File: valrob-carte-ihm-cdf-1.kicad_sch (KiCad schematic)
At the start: 42 parts, among them J1 USB_C_Receptacle_USB2.0_14P, J2 Conn_01x02, J3 Conn_01x02, J4 Conn_01x04_Pin, J5 Conn_01x04_Pin, J6 Conn_01x04_Pin, SW1 SW_Push, SW2 SW_Push, SW3 SW_DIP_x04, U1 TLV75733PDBV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

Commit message: pcb: add display buttons routing
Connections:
- net SCL: now also U4.15 (GPIO3/TOUCH3/ADC1_CH2); no longer U4.12 (GPIO8/TOUCH8/ADC1_CH7/SUBSPICS1)

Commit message: pcb: add toggle switch routing
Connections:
- net RGB_LEDS: now also U4.22 (GPIO14/TOUCH14/ADC2_CH3/FSPIWP/FSPIDQS/SUBSPIWP); no longer U4.18 (GPIO10/TOUCH10/ADC1_CH9/FSPICS0/FSPIIO4/SUBSPICS0)
- net Switches/ESW2: now also U4.21 (GPIO13/TOUCH13/ADC2_CH2/FSPIQ/FSPIIO7/SUBSPIQ); no longer U4.20 (GPIO12/TOUCH12/ADC2_CH1/FSPICLK/FSPIIO6/SUBSPICLK)
- net Switches/ESW3: now also U4.20 (GPIO12/TOUCH12/ADC2_CH1/FSPICLK/FSPIIO6/SUBSPICLK); no longer U4.21 (GPIO13/TOUCH13/ADC2_CH2/FSPIQ/FSPIIO7/SUBSPIQ)
- net Switches/ESW4: now also U4.18 (GPIO10/TOUCH10/ADC1_CH9/FSPICS0/FSPIIO4/SUBSPICS0); no longer U4.22 (GPIO14/TOUCH14/ADC2_CH3/FSPIWP/FSPIDQS/SUBSPIWP)

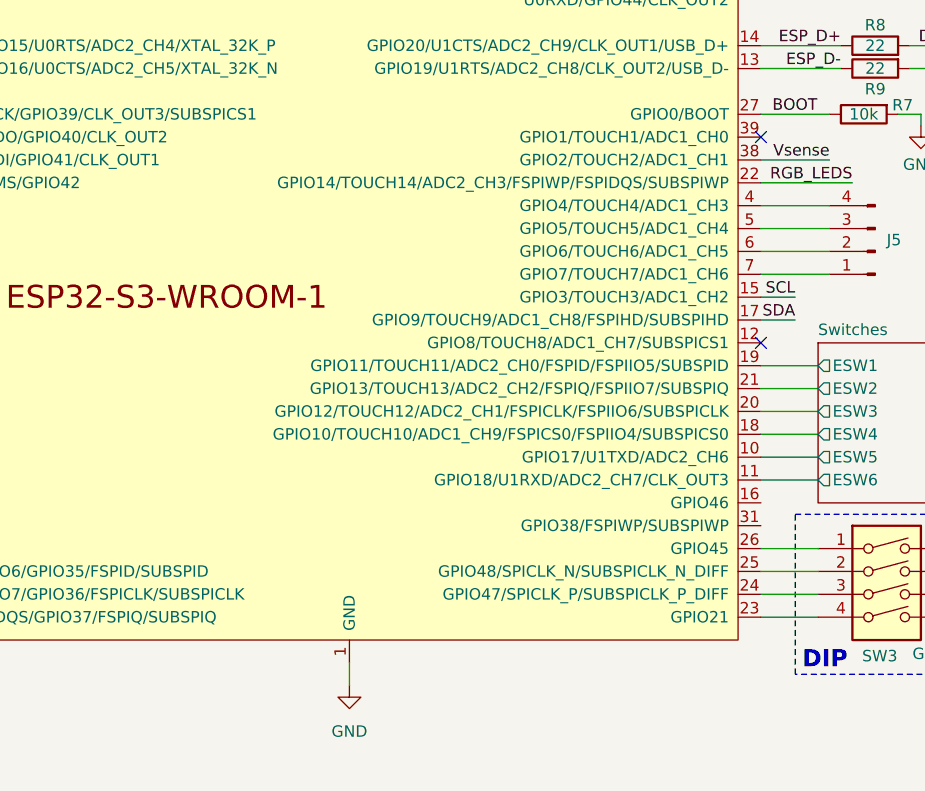
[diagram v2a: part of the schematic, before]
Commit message: pcb: add DIP switches routing
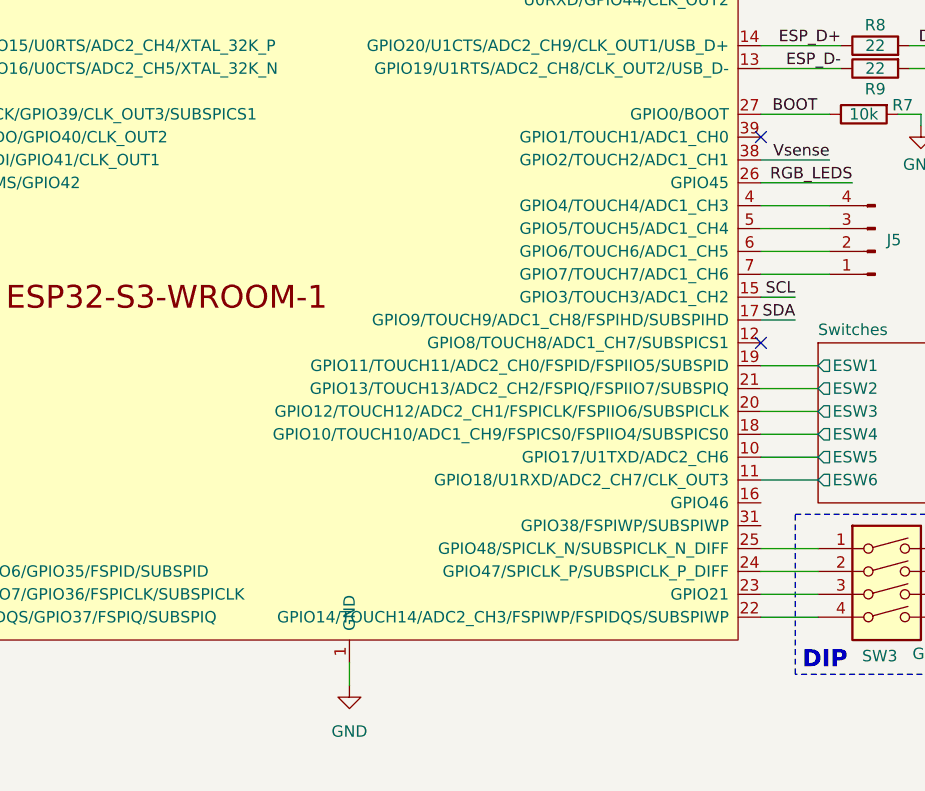
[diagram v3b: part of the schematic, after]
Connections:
- net RGB_LEDS: now also U4.26 (GPIO45); no longer U4.22 (GPIO14/TOUCH14/ADC2_CH3/FSPIWP/FSPIDQS/SUBSPIWP)
- net at SW3.4: now also U4.22 (GPIO14/TOUCH14/ADC2_CH3/FSPIWP/FSPIDQS/SUBSPIWP); no longer U4.23 (GPIO21)
- net at SW3.3: now also U4.23 (GPIO21); no longer U4.24 (GPIO47/SPICLK_P/SUBSPICLK_P_DIFF)
- net at SW3.2: now also U4.24 (GPIO47/SPICLK_P/SUBSPICLK_P_DIFF); no longer U4.25 (GPIO48/SPICLK_N/SUBSPICLK_N_DIFF)
- net at SW3.1: now also U4.25 (GPIO48/SPICLK_N/SUBSPICLK_N_DIFF); no longer U4.26 (GPIO45)

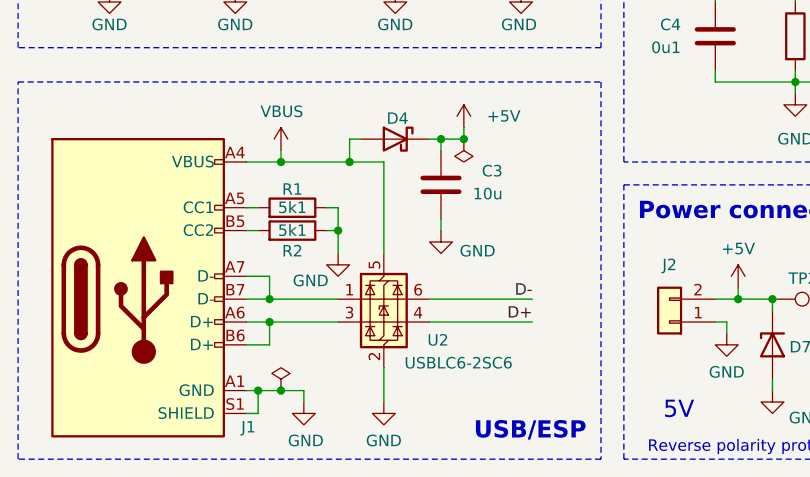
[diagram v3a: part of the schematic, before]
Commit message: switch ST usb ESD to H5VU10U tvs diodes
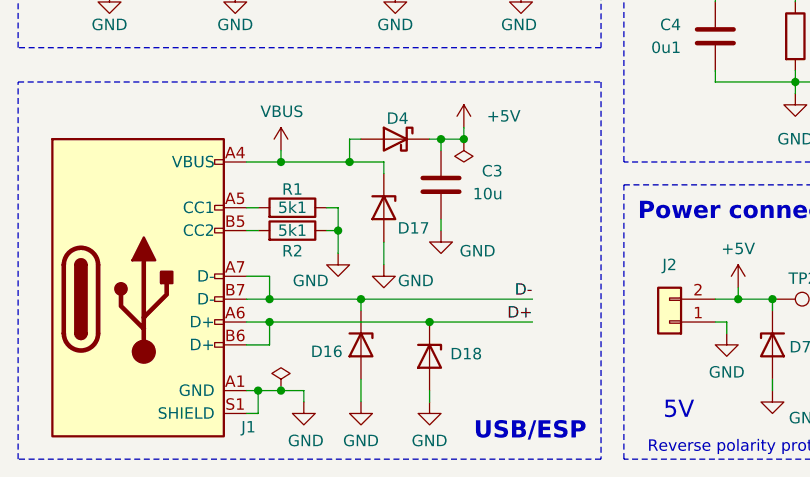
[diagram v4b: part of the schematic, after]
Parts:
- removed U2: USBLC6-2SC6, Package_TO_SOT_SMD:SOT-23-6, symbol Power_Protection:USBLC6-2SC6
- added D16, D17, D18: H5VU10U, Pers:Diode_DFN1006, symbol Pers:H5VU10U
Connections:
- net D+: now also J1.A6 (D+), J1.B6 (D+), D18.1 (K)
- net D-: now also J1.A7 (D-), J1.B7 (D-), D16.1 (K)
- net GND: now also D16.2 (A), D17.2 (A), D18.2 (A)
- net VBUS: now also D17.1 (K)

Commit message: add production files
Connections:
- no-connect marks 8 -> 10
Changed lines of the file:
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@@
+	)
+	(no_connect
+		(at 246.38 115.57)
 	)
 	(no_connect
@@
 	)
 	(no_connect
+		(at 246.38 118.11)
+	)
+	(no_connect

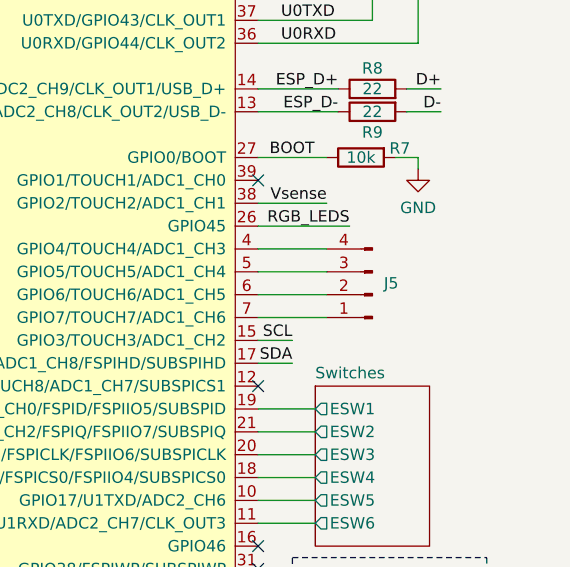
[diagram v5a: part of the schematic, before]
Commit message: pcb/schem: add missing i2c external pullups
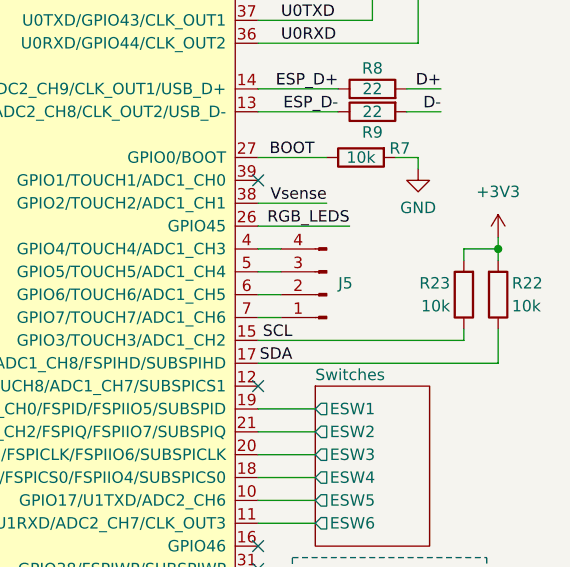
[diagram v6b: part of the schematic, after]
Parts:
- added R22, R23: 10k, Resistor_SMD:R_0402_1005Metric, symbol Device:R
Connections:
- net +3V3: now also R22.2, R23.2
- net SCL: now also R23.1
- net SDA: now also R22.1
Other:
- moved on the sheet: J5

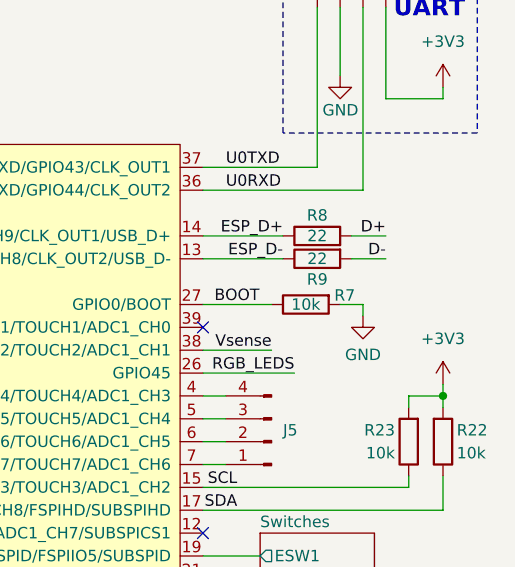
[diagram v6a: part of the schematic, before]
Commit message: pcb/schem: fix BOOT pullup
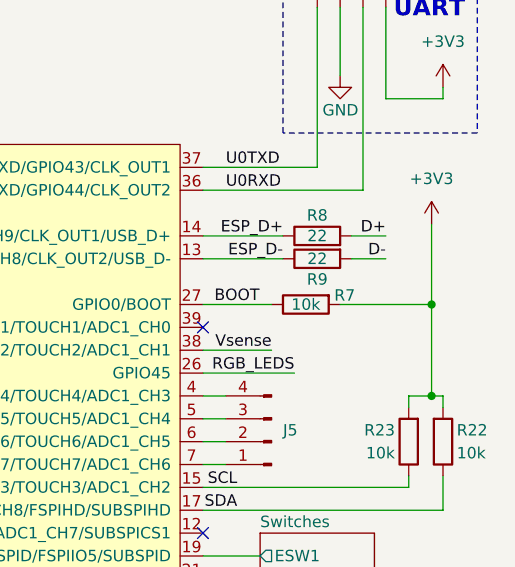
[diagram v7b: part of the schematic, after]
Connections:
- net +3V3: now also R7.2
- net GND: no longer R7.2
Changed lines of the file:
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@@
 	)
 	(junction
-		(at 273.05 82.55)
+		(at 271.78 82.55)
 		(diameter 0)
 		(color 0 0 0 0)
@@
 	)
 	(junction
+		(at 271.78 72.39)
+		(diameter 0)
+		(color 0 0 0 0)
+	)
+	(junction
 		(at 50.8 168.91)
 		(diameter 0)
@@
 	(wire
 		(pts
+			(xy 261.62 72.39) (xy 271.78 72.39)
+		)
+		(stroke
+			(width 0)
+			(type default)
+		)
+	)
+	(wire
+		(pts
 			(xy 246.38 125.73) (xy 252.73 125.73)
 		)
@@
 	(wire
 		(pts
+			(xy 271.78 72.39) (xy 271.78 82.55)
+		)
+		(stroke
+			(width 0)
+			(type default)
+		)
+	)
+	(wire
+		(pts
 			(xy 50.8 125.73) (xy 50.8 130.81)
 		)
@@
 	(wire
 		(pts
-			(xy 273.05 81.28) (xy 273.05 82.55)
+			(xy 271.78 63.5) (xy 271.78 72.39)
 		)
 		(stroke
@@
 	(wire
 		(pts
-			(xy 264.16 73.66) (xy 264.16 72.39)
-		)
-		(stroke
-			(width 0)
-			(type default)
-		)
-	)
-	(wire
-		(pts
 			(xy 64.77 158.75) (xy 64.77 157.48)
 		)
@@
 	(wire
 		(pts
-			(xy 264.16 72.39) (xy 261.62 72.39)
-		)
-		(stroke
-			(width 0)
-			(type default)
-		)
-	)
-	(wire
-		(pts
 			(xy 59.69 99.06) (xy 60.96 99.06)
 		)
@@
 	(wire
 		(pts
-			(xy 273.05 82.55) (xy 269.24 82.55)
+			(xy 273.05 82.55) (xy 271.78 82.55)
 		)
 		(stroke
@@
 	(wire
 		(pts
+			(xy 269.24 82.55) (xy 271.78 82.55)
+		)
+		(stroke
+			(width 0)
+			(type default)
+		)
+	)
+	(wire
+		(pts
 			(xy 68.58 107.95) (xy 52.07 107.95)
 		)
@@
 	(symbol
 		(lib_id "power:GND")
-		(at 264.16 73.66 0)
-		(unit 1)
-		(exclude_from_sim no)
-		(in_bom yes)
-		(on_board yes)
-		(dnp no)
-		(property "Reference" "#PWR032"
-			(at 264.16 80.01 0)
-			(effects
-				(font
-					(size 1.27 1.27)
-				)
-				(hide yes)
-			)
-		)
-		(property "Value" "GND"
-			(at 264.16 77.978 0)
-			(effects
-				(font
-					(size 1.27 1.27)
-				)
-			)
-		)
-		(property "Footprint" ""
-			(at 264.16 73.66 0)
-			(effects
-				(font
-					(size 1.27 1.27)
-				)
-				(hide yes)
-			)
-		)
-		(property "Datasheet" ""
-			(at 264.16 73.66 0)
-			(effects
-				(font
-					(size 1.27 1.27)
-				)
-				(hide yes)
-			)
-		)
-		(property "Description" "Power symbol creates a global label with name \"GND\" , ground"
-			(at 264.16 73.66 0)
-			(effects
-				(font
-					(size 1.27 1.27)
-				)
-				(hide yes)
-			)
-		)
-		(pin "1"
-		)
-		(instances
-			(project "valrob-carte-ihm-cdf-1"
-				(path "/59430078-5c05-41f6-b5ab-2c89bd050ea6"
-					(reference "#PWR032")
-					(unit 1)
-				)
-			)
-		)
-	)
-	(symbol
-		(lib_id "power:GND")
 		(at 114.3 124.46 0)
 		(unit 1)
@@
 	(symbol
 		(lib_id "power:+3V3")
-		(at 273.05 81.28 0)
+		(at 271.78 63.5 0)
 		(unit 1)
 		(exclude_from_sim no)
@@
 		(fields_autoplaced yes)
 		(property "Reference" "#PWR062"
-			(at 273.05 85.09 0)
+			(at 271.78 67.31 0)
 			(effects
 				(font
@@
 		)
 		(property "Value" "+3V3"
-			(at 273.05 76.2 0)
+			(at 271.78 58.42 0)
 			(effects
 				(font
@@
 		)
 		(property "Footprint" ""
-			(at 273.05 81.28 0)
+			(at 271.78 63.5 0)
 			(effects
 				(font
@@
 		)
 		(property "Datasheet" ""
-			(at 273.05 81.28 0)
+			(at 271.78 63.5 0)
 			(effects
 				(font
@@
 		)
 		(property "Description" "Power symbol creates a global label with name \"+3V3\""
-			(at 273.05 81.28 0)
+			(at 271.78 63.5 0)
 			(effects
 				(font
